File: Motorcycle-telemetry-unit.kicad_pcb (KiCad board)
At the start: 2 copper layers, 133.8 x 95.4 mm, 109 parts, among them J1 USB_B_Micro-ESP32, J2 Screw_Terminal_01x02, J3 Screw_Terminal_01x02, J4 Micro_SD_Card_Det, J5 GoPro Power USBAx2, J6 Screw_Terminal_01x10, K1 ADW11, Q1 Q_PMOS_DGS, Q2 Q_NMOS_DGS, Q3 Q_PMOS_DGS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

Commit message: Fixes and updates
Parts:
- moved R32 5.74 mm to (158.8, 71.0)
- moved R31 4.17 mm to (163.6, 70.9)
- moved R36 2.95 mm to (158.8, 63.7), turned to -90 degrees
- moved R39 2.90 mm to (163.6, 63.7), turned to -90 degrees
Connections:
- net /12v-LED-CAT renamed /12v-LED-CATH
- net /5v-In renamed /5v-IN
- net /CHARGING-LED-CAT renamed /CHARGING-LED-CATH
- net Net-(D4-Pad1) renamed /5v-LED-CATH
- net Net-(D6-Pad1) renamed /3.3v-LED-CATH
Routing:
- net GND: track 829.0 -> 886.7 mm, vias 27 -> 28
- net /TR_RIGT: track 56.9 -> 0.00 mm
- net /TR_LEFT: track 49.5 -> 0.00 mm
- net /BR_REAR: track 44.2 -> 0.00 mm
- net /BR_FRNT: track 39.5 -> 0.00 mm
- net +3V3: track 466.8 -> 434.1 mm
- net Net-(J1-Pad2): track 11.9 -> 44.2 mm, vias 0 -> 2
- net Net-(J1-Pad3): track 19.7 -> 50.1 mm, vias 0 -> 2
- net /H_SDA: track 45.0 -> 71.3 mm
- net /H_SCL: track 41.4 -> 66.9 mm
- net /E_SCL: track 0.00 -> 13.6 mm
- net /E_SDA: track 0.00 -> 8.80 mm
- net /KICK: track 62.8 -> 61.8 mm
- net ~{RESET}: track 121.3 -> 120.3 mm
- net Net-(C1-Pad1): track 6.37 -> 5.47 mm
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
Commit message: Update Motorcycle-telemetry-unit.kicad_pcb
Wiring
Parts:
- moved C3 1.53 mm to (145.4, 60.4)
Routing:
- net /H_SCL: track 66.9 -> 164.4 mm, vias 3 -> 8
- net /H_SDA: track 71.3 -> 161.6 mm, vias 3 -> 7
- net +3V3: track 434.1 -> 391.0 mm, vias 3 -> 4
- net /E_SCL: track 13.6 -> 25.4 mm, vias 0 -> 2
- net /E_SDA: track 8.80 -> 19.4 mm, vias 0 -> 2
- net Net-(C3-Pad1): track 11.9 -> 15.4 mm
- net GND: track 886.7 -> 888.3 mm
- net Net-(AE1-Pad1): track 5.71 -> 7.25 mm
- net Net-(R37-Pad2): track 17.0 -> 17.6 mm

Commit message: More clean up
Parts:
- Q1, Q2, Q3, Q4: footprint Package_TO_SOT_THT:TO-220-3_Vertical -> Package_TO_SOT_SMD:SOT-23
- moved Q2 3.05 mm to (141.9, 121.9), turned to 90 degrees
- moved Q4 1.42 mm to (156.5, 122.4), turned to 90 degrees
- moved Q3 1.34 mm to (157.2, 110.3), turned to 90 degrees
- moved Q1 1.30 mm to (140.6, 110.3), turned to 90 degrees
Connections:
- net Charge-Sens renamed /5V-OUT
- net Net-(AE1-Pad1) renamed /ANT.
- Q3 pad 3: unconnected-(Q3-Pad3) -> +3V3
- U10 pad 4: unconnected-(U10-Pad4) -> IMU_BOOTN
- U11 pad 17: unconnected-(U11-Pad17) -> IMU_BOOTN
- U11 pad 18: unconnected-(U11-Pad18) -> HOST_INT
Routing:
- net Recharge_Arm: track 3.99 -> 27.5 mm, vias 0 -> 2
- net Recharge_Disarm: track 3.99 -> 25.9 mm
- net +3V3: track 391.0 -> 402.9 mm
- net GND: track 888.3 -> 896.4 mm
- net Recharge_Set: track 27.0 -> 28.9 mm

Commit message: wired
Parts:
- moved C4 3.86 mm to (142.6, 65.3)
- moved C3 2.90 mm to (142.5, 60.5)
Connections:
- J5 pad 1: +5V -> /5V-OUT
- J5 pad 5: +5V -> /5V-OUT
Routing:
- net +5V: track 68.5 -> 237.0 mm, vias 0 -> 1
- net +12V: track 19.9 -> 157.2 mm
- net +3V3: track 402.9 -> 442.4 mm
- net /H_SDA: track 161.6 -> 200.7 mm
- net /5V-OUT: track 98.9 -> 124.8 mm
- net /H_SCL: track 164.4 -> 190.3 mm
- net GND: track 896.4 -> 921.4 mm, vias 28 -> 30
- net /BIKE_BATT: track 215.2 -> 227.3 mm
- net Net-(C3-Pad1): track 15.4 -> 18.2 mm
- net Net-(R37-Pad2): track 17.6 -> 16.8 mm

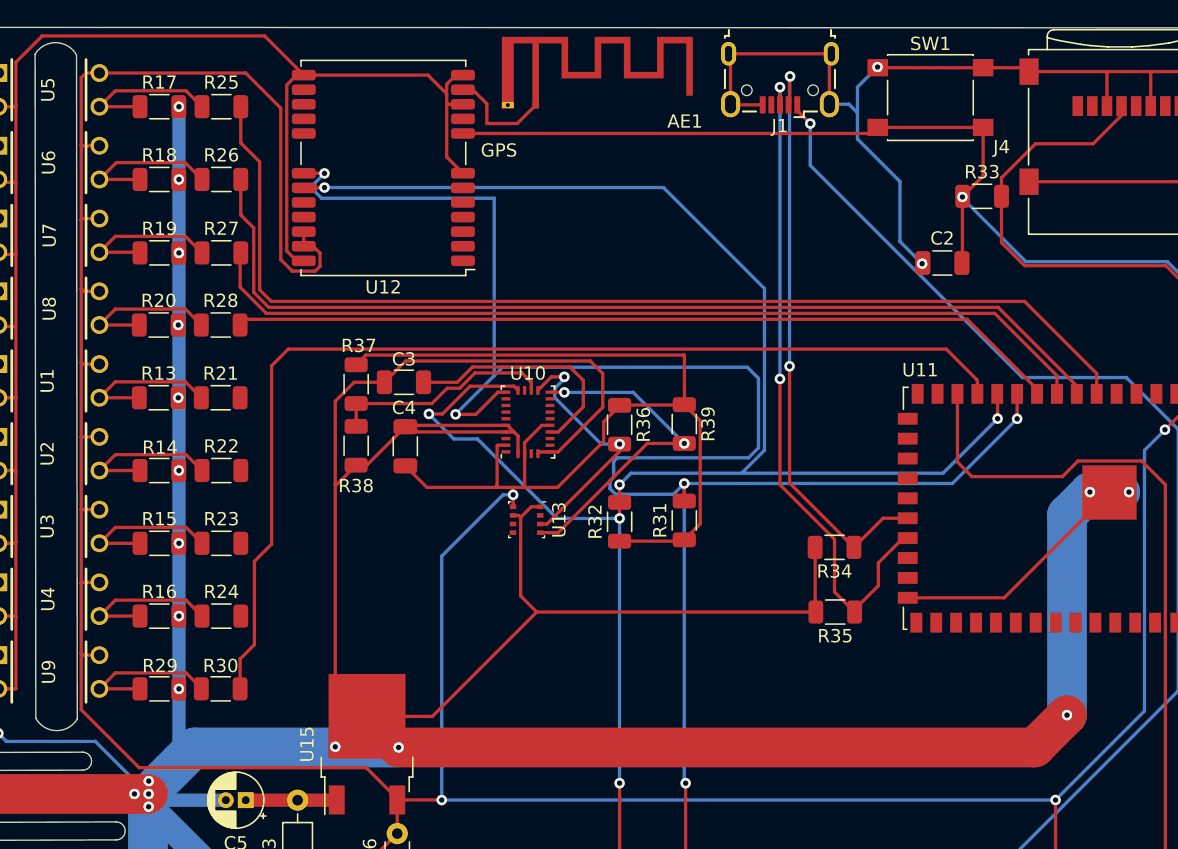
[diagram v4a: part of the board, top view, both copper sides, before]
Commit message: Corrections to optoarray
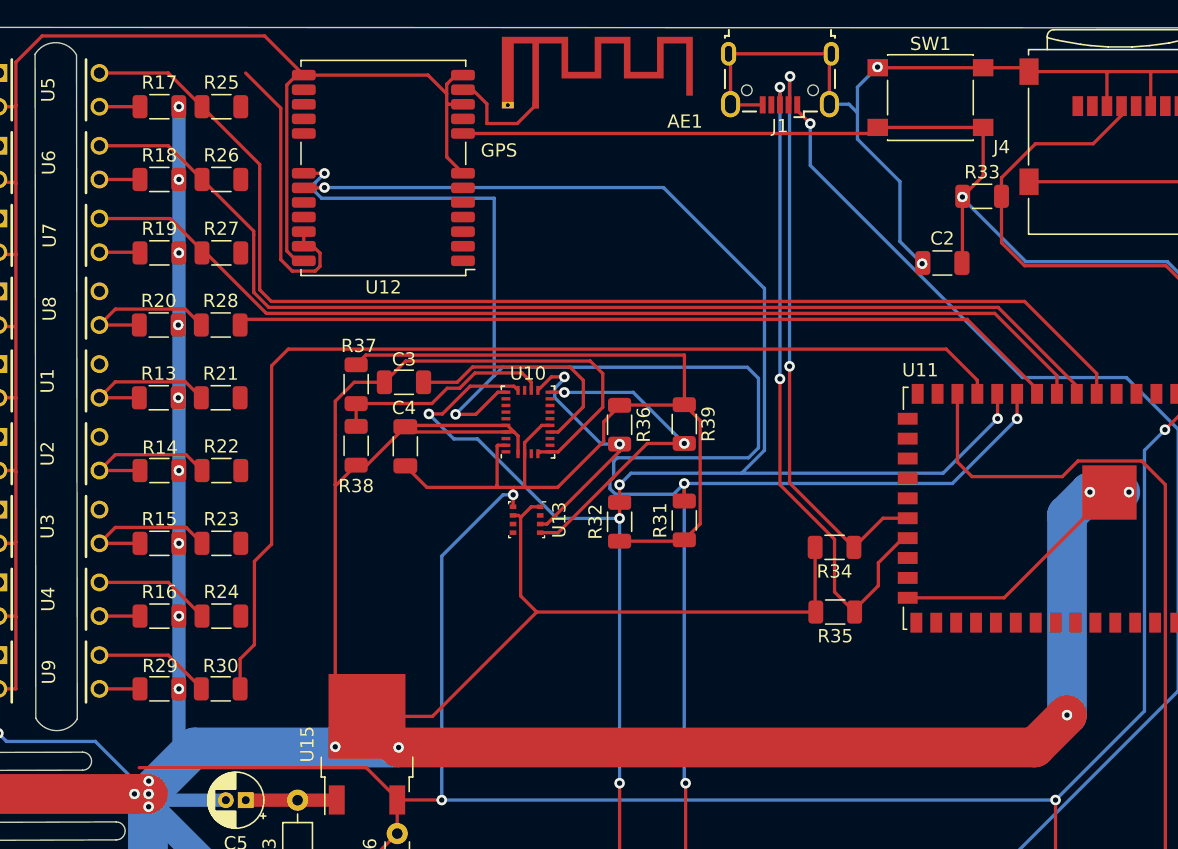
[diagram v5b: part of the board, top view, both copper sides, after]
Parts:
- C1: value C_Small -> 0.1uF
- R10, R3, R4, R5, R6, R7, R9: value R_US -> 300R
- R13, R14, R15, R16, R17, R18, R19, R20, R29: value R_Small_US -> 0R
- R21, R23, R24, R25, R26, R27, R28, R30: value R_US -> 10k
- R22: value R_US -> 0R
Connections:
- R21 pad 1: Net-(R13-Pad1) -> /BR_FRNT
- R21 pad 2: /BR_FRNT -> +3V3
- R22 pad 1: Net-(R14-Pad1) -> /BR_REAR
- R22 pad 2: /BR_REAR -> +3V3
- R23 pad 1: Net-(R15-Pad1) -> /TR_LEFT
- R23 pad 2: /TR_LEFT -> +3V3
- R24 pad 1: Net-(R16-Pad1) -> /TR_RIGT
- R24 pad 2: /TR_RIGT -> +3V3
- R25 pad 1: Net-(R17-Pad1) -> /IGN
- R25 pad 2: /IGN -> +3V3
- R26 pad 1: Net-(R18-Pad1) -> /START
- R26 pad 2: /START -> +3V3
- R27 pad 1: Net-(R19-Pad1) -> /NEUTRAL
- R27 pad 2: /NEUTRAL -> +3V3
- R28 pad 1: Net-(R20-Pad1) -> /KICK
- R28 pad 2: /KICK -> +3V3
- R30 pad 1: Net-(R29-Pad1) -> /TACH
- R30 pad 2: /TACH -> +3V3
- U1 pad 4: +3V3 -> /BR_FRNT
- U2 pad 4: +3V3 -> /BR_REAR
- U3 pad 4: +3V3 -> /TR_LEFT
- U4 pad 4: +3V3 -> /TR_RIGT
- U5 pad 4: +3V3 -> /IGN
- U6 pad 4: +3V3 -> /START
- U7 pad 4: +3V3 -> /NEUTRAL
- U8 pad 4: +3V3 -> /KICK
- U9 pad 4: +3V3 -> /TACH
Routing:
- net /TACH: track 81.1 -> 8.76 mm
- net /NEUTRAL: track 68.4 -> 78.6 mm
- net /START: track 73.9 -> 83.9 mm
- net /IGN: track 81.7 -> 91.6 mm
- net /TR_RIGT: track 0.00 -> 8.79 mm
- net Net-(R18-Pad1): track 11.8 -> 3.06 mm
- net Net-(R17-Pad1): track 11.8 -> 3.06 mm
- net Net-(R16-Pad1): track 11.8 -> 3.06 mm
- net Net-(R19-Pad1): track 11.7 -> 3.01 mm
- net Net-(R29-Pad1): track 11.7 -> 3.06 mm
- net +3V3: track 442.4 -> 445.9 mm
